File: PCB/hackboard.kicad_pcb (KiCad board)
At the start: 2 copper layers, 360.4 x 130.4 mm, 162 parts, among them SW1 SW_Push, SW10 SW_Push, SW11 SW_Push, SW12 SW_Push, SW13 SW_Push, SW14 SW_Push, SW15 SW_Push, SW16 SW_Push, SW17 SW_Push, SW18 SW_Push, SW19 SW_Push, SW2 SW_Push, SW20 SW_Push, SW21 SW_Push, SW22 SW_Push, SW23 SW_Push, SW24 SW_Push, SW25 SW_Push, SW26 SW_Push, SW27 SW_Push, SW28 SW_Push, SW29 SW_Push, SW3 SW_Push, SW30 SW_Push, SW31 SW_Push, SW32 SW_Push, SW33 SW_Push, SW34 SW_Push, SW35 SW_Push, SW36 SW_Push, SW37 SW_Push, SW38 SW_Push, SW39 SW_Push, SW4 SW_Push, SW40 SW_Push, SW41 SW_Push, SW42 SW_Push, SW43 SW_Push, SW44 SW_Push, SW45 SW_Push, SW46 SW_Push, SW47 SW_Push, SW48 SW_Push, SW49 SW_Push, SW5 SW_Push, SW50 SW_Push, SW51 SW_Push, SW52 SW_Push, SW53 SW_Push, SW54 SW_Push, SW55 SW_Push, SW56 SW_Push, SW57 SW_Push, SW58 SW_Push, SW59 SW_Push, SW6 SW_Push, SW60 SW_Push, SW61 SW_Push, SW62 SW_Push, SW63 SW_Push, SW64 SW_Push, SW65 SW_Push, SW66 SW_Push, SW67 SW_Push, SW68 SW_Push, SW69 SW_Push, SW7 SW_Push, SW70 SW_Push, SW71 SW_Push, SW72 SW_Push, SW73 SW_Push, SW74 SW_Push, SW75 SW_Push, SW76 SW_Push, SW77 SW_Push, SW78 SW_Push, SW79 RotaryEncoder_Switch, SW8 SW_Push, SW9 SW_Push, U1 Pico

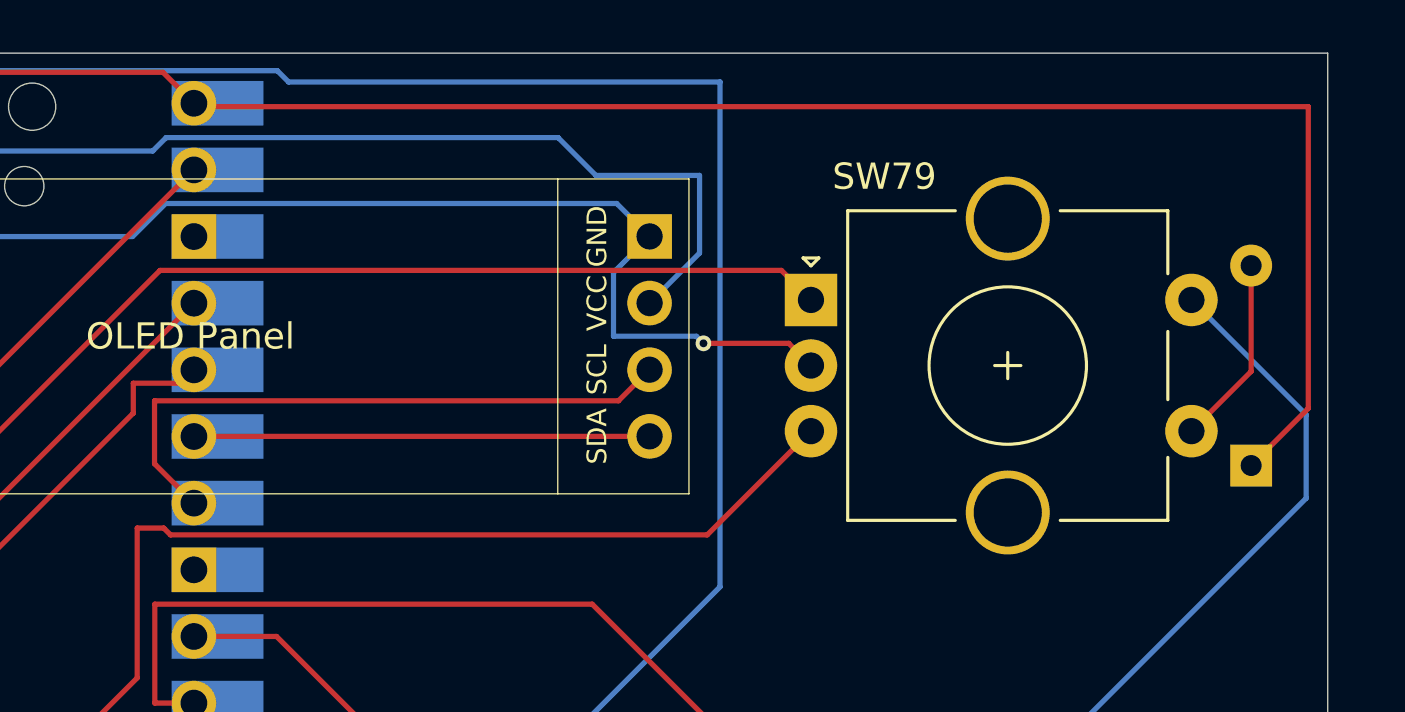
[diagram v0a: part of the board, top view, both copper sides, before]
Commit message: updated Case and made padding thinner
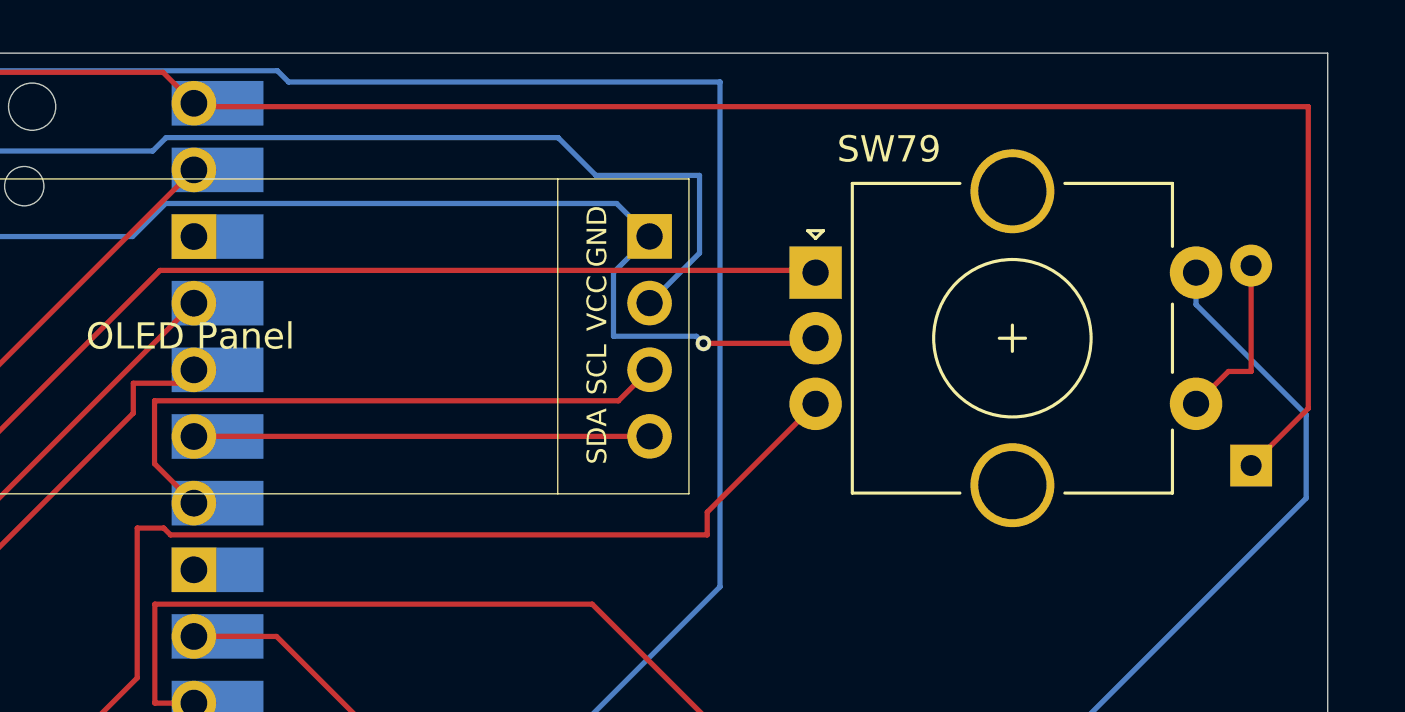
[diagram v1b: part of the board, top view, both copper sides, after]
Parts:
- moved SW79 1.06 mm to (370.2, 84.5)
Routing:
- net enc1: track 54.5 -> 55.6 mm
- net col14: track 127.9 -> 128.9 mm
- net Net-(D85-A): track 7.25 -> 6.64 mm
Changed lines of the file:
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@@
 	(footprint "hc_lib:RotaryEncoder_Alps_EC11E-Switch_Vertical_H20mm_CircularMountingHoles_3D"
 		(layer "F.Cu")
-		(at 370.07375 85.54125)
+		(at 370.25 84.5)
 		(descr "Alps rotary encoder, EC12E... with switch, vertical shaft, mounting holes with circular drills, http://www.alps.com/prod/info/E/HTML/Encoder/Incremental/EC11/EC11E15204A3.html")
 		(tags "rotary encoder")
@@
 	(segment
 		(start 365.9775 87.195)
-		(end 369.2275 87.195)
+		(end 370.055 87.195)
 		(width 0.2)
 		(layer "F.Cu")
@@
 	)
 	(segment
-		(start 369.2275 87.195)
-		(end 370.07375 88.04125)
+		(start 370.055 87.195)
+		(end 370.25 87)
 		(width 0.2)
 		(layer "F.Cu")
@@
 	(segment
 		(start 386.84875 88.26625)
-		(end 384.57375 90.54125)
+		(end 385.98375 88.26625)
+		(width 0.2)
+		(layer "F.Cu")
+		(net 90)
+	)
+	(segment
+		(start 385.98375 88.26625)
+		(end 384.75 89.5)
 		(width 0.2)
 		(layer "F.Cu")
@@
 	)
 	(segment
-		(start 306.73 114.225)
-		(end 303.77 111.265)
+		(start 388.9475 89.915)
+		(end 384.75 85.7175)
 		(width 0.2)
 		(layer "B.Cu")
@@
 	)
 	(segment
-		(start 388.9475 89.915)
-		(end 384.57375 85.54125)
+		(start 306.73 114.225)
+		(end 303.77 111.265)
 		(width 0.2)
 		(layer "B.Cu")
@@
 	)
 	(segment
+		(start 384.75 85.7175)
+		(end 384.75 84.5)
+		(width 0.2)
+		(layer "B.Cu")
+		(net 104)
+	)
+	(segment
 		(start 314.7875 111.065)
 		(end 311.6275 114.225)
@@
 	)
 	(segment
-		(start 331.4675 102.325)
-		(end 331.4675 98.215)
+		(start 345.2675 84.415)
+		(end 370.165 84.415)
 		(width 0.2)
 		(layer "F.Cu")
@@
 	)
 	(segment
-		(start 331.4675 98.215)
-		(end 345.2675 84.415)
+		(start 370.165 84.415)
+		(end 370.25 84.5)
 		(width 0.2)
 		(layer "F.Cu")
@@
 	)
 	(segment
-		(start 368.9475 84.415)
-		(end 370.07375 85.54125)
+		(start 331.4675 98.215)
+		(end 345.2675 84.415)
 		(width 0.2)
 		(layer "F.Cu")
@@
 	)
 	(segment
-		(start 345.2675 84.415)
-		(end 368.9475 84.415)
+		(start 331.4675 102.325)
+		(end 331.4675 98.215)
 		(width 0.2)
 		(layer "F.Cu")
@@
 	)
 	(segment
-		(start 345.4075 94.235)
-		(end 345.6675 94.495)
+		(start 366.12 94.495)
+		(end 366.12 93.63)
 		(width 0.2)
 		(layer "F.Cu")
@@
 	)
 	(segment
-		(start 366.12 94.495)
-		(end 370.07375 90.54125)
+		(start 366.12 93.63)
+		(end 370.25 89.5)
+		(width 0.2)
+		(layer "F.Cu")
+		(net 106)
+	)
+	(segment
+		(start 345.4075 94.235)
+		(end 345.6675 94.495)
 		(width 0.2)
 		(layer "F.Cu")

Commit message: split case into 2, recompile STL and STEP files
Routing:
- net row5: track 381.9 -> 391.4 mm
- net row1: track 644.2 -> 646.4 mm
- net row6: track 458.7 -> 460.3 mm
- net GND: track 48.5 -> 49.3 mm
- net col7: track 334.2 -> 333.5 mm
